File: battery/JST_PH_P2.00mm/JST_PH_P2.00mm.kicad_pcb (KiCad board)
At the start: 2 copper layers, 1 part

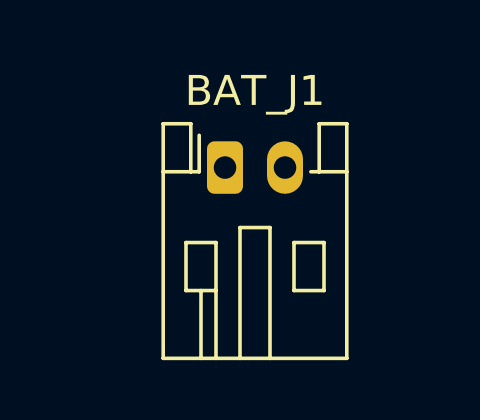
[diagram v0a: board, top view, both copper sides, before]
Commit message: update power switch
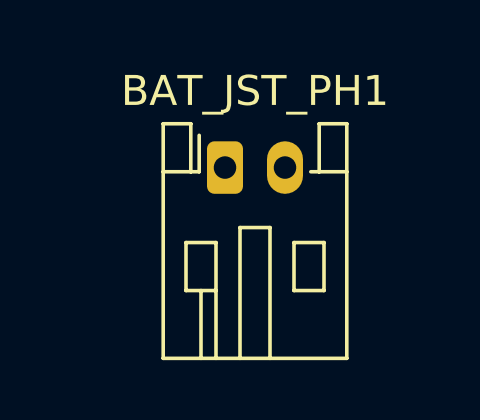
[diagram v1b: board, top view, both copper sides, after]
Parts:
- removed BAT_J1: BATT, ErgoCai.pretty:JST_PH_S2B-PH-K_1x02_P2.00mm_Horizontal
- added BAT_JST_PH1: BATT, ErgoCai.pretty:JST_PH_S2B-PH-K_1x02_P2.00mm_Horizontal, F.Cu at (0.00, 0.00)

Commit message: correct JST_PH_P2.00mm pos
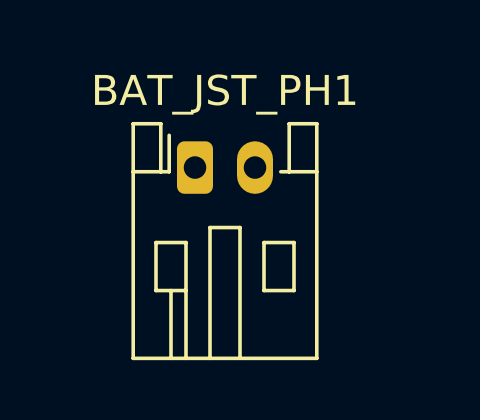
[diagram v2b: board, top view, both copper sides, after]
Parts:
- moved BAT_JST_PH1 1.00 mm to (-1.00, 0.00)
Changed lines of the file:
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@@
 	(footprint "ErgoCai.pretty:JST_PH_S2B-PH-K_1x02_P2.00mm_Horizontal"
 		(layer "F.Cu")
-		(at 0 0)
+		(at -1 0)
 		(descr "JST PH series connector, S2B-PH-K (http://www.jst-mfg.com/product/pdf/eng/ePH.pdf), generated with kicad-footprint-generator")
 		(tags "connector JST PH horizontal")
